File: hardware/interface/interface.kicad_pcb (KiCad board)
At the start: 2 copper layers, 44.4 x 35.6 mm, 7 parts, among them J1 Board Connector, SW1 Rotary_Encoder_Switch, U1 128x32_OLED, U2 MCP23018-E_SS

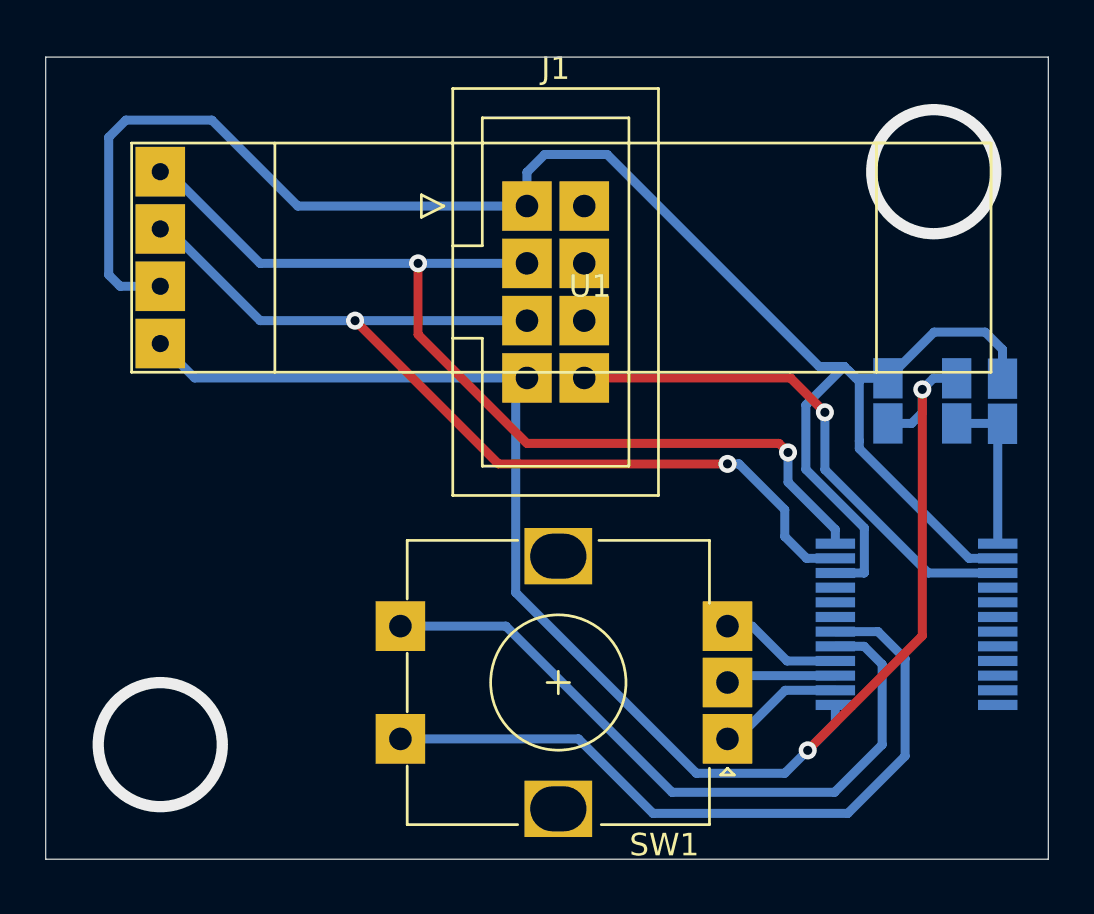
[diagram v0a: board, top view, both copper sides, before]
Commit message: Fixing via sizes.
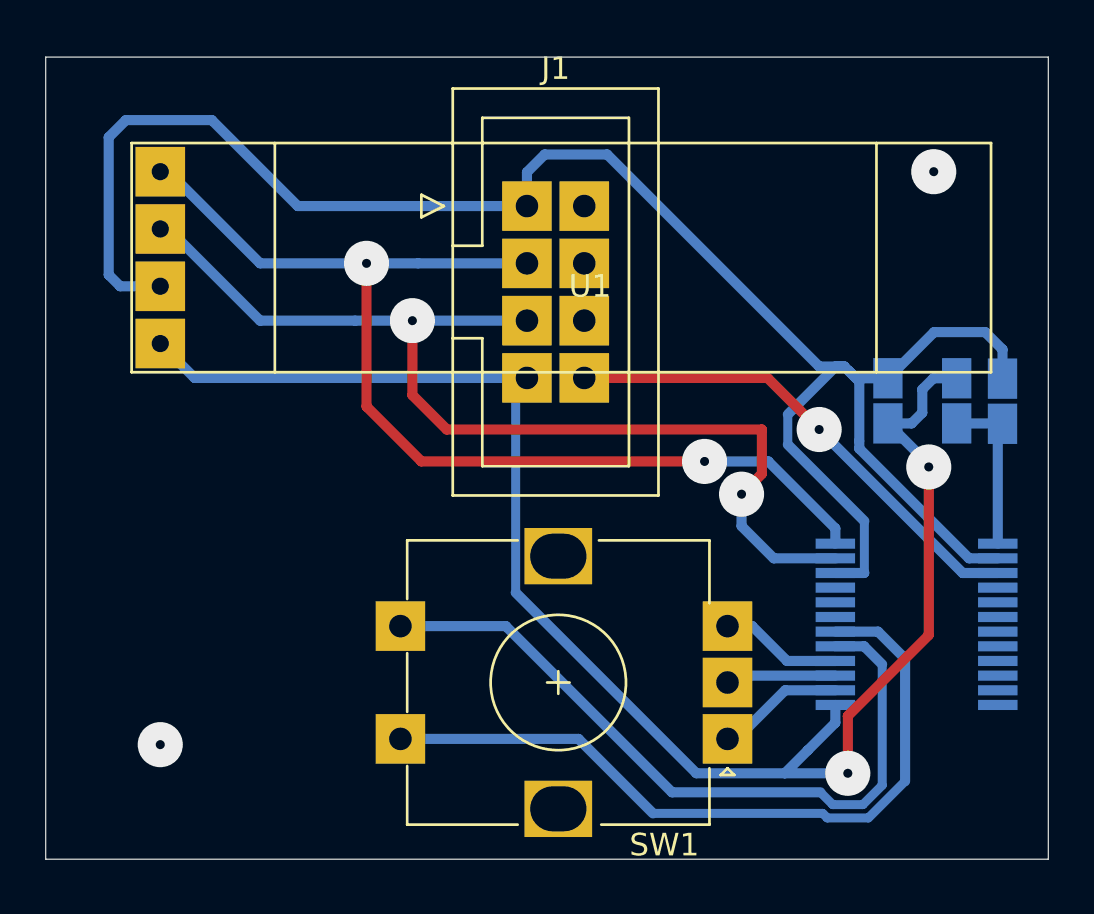
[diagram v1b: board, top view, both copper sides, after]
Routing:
- net SDA: track 44.6 -> 48.0 mm
- net SCL: track 44.3 -> 46.8 mm
- net GND: track 68.4 -> 70.8 mm
- net Net-(SW1-PadS2): track 31.3 -> 32.8 mm
- net INT: track 23.4 -> 21.9 mm
- net +5V: track 82.5 -> 83.4 mm
- net Net-(SW1-PadS1): track 32.7 -> 33.5 mm
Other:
- net class Default: trace_width 0.4 -> 0.45; via_dia 0.8 -> 2
